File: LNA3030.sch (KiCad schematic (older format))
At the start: 25 parts, among them P1 SMA-KIT-1.5MF, U1 SWITCH, U2 SWITCH, U3 LNA, U4 SAW

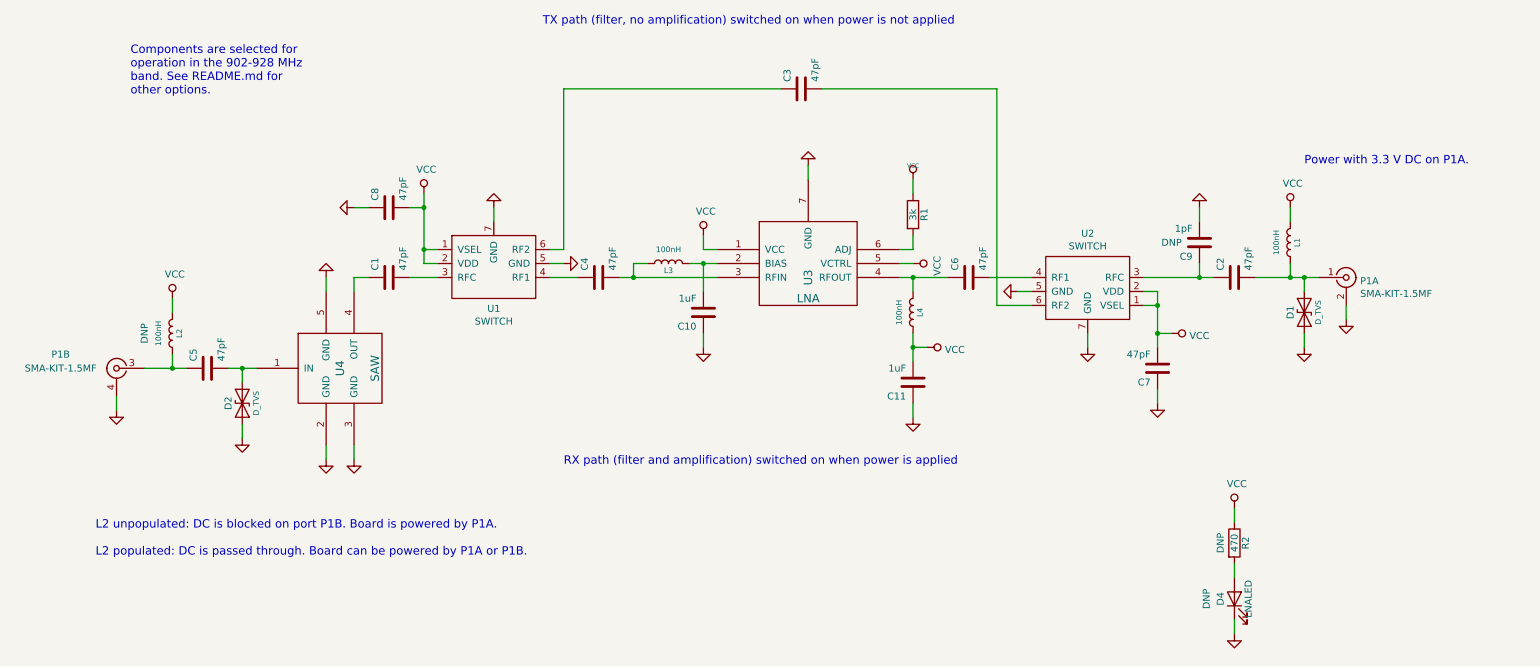
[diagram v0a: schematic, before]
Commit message: modify for DCC6C SAW filters
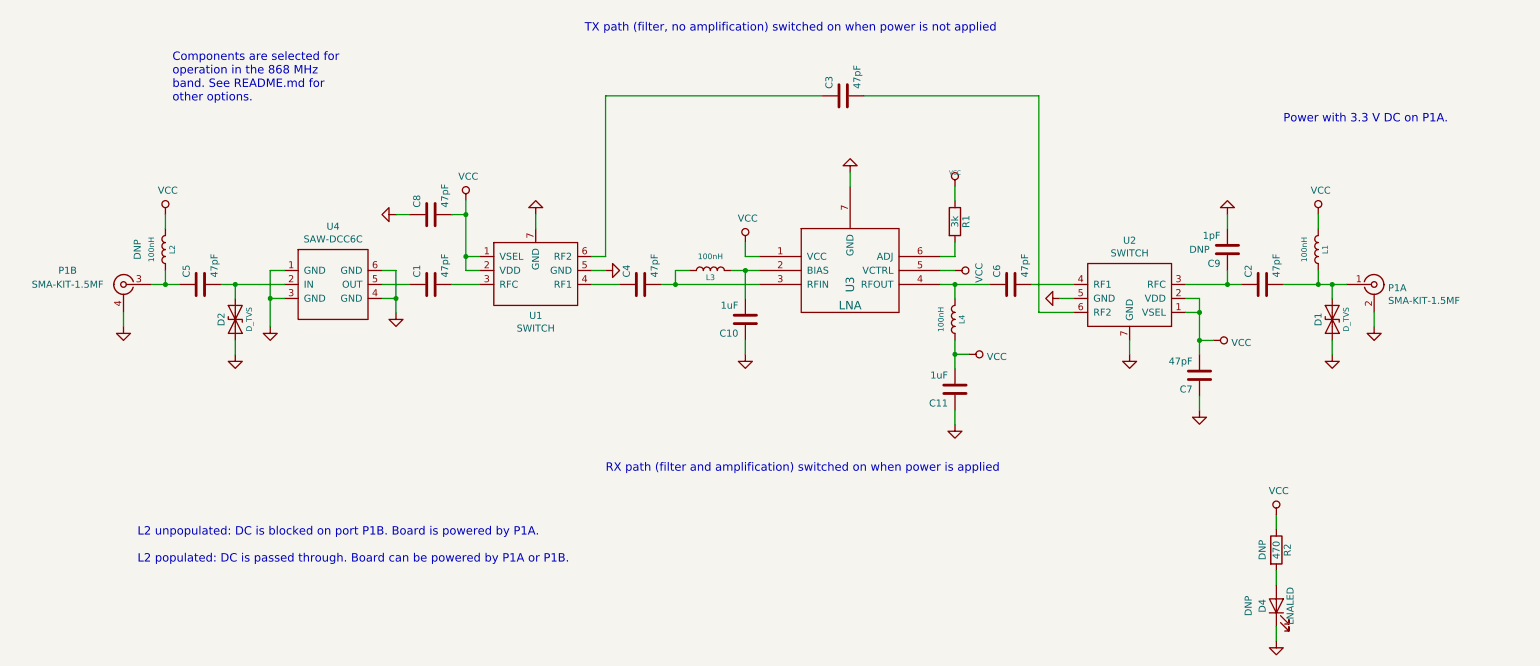
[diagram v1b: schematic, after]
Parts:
- removed U4: SAW, gsg-modules:F5Q, symbol gsg-symbols:FAR-F5QA
- added U4: SAW-DCC6C, LNA3030:DCC6C, symbol LNA3030:SAW-DCC6C
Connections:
- net GND: now also U4.1 (GND), U4.3 (GND), U4.4 (GND), U4.6 (GND)
- net at C5.2, D2.2 (A2): now also U4.2 (IN)
- net at C1.1: now also U4.5 (OUT)
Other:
- note added: "Components are selected for\noperation in the 868 MHz\nband. See README.md for\nother options."
- note removed: "Components are selected for\noperation in the 902-928 MHz\nband. See README.md for\nother options."
- moved on the sheet: C1, C10, C11, C2, C3, C4, C5, C6, C7, C8, C9, D1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

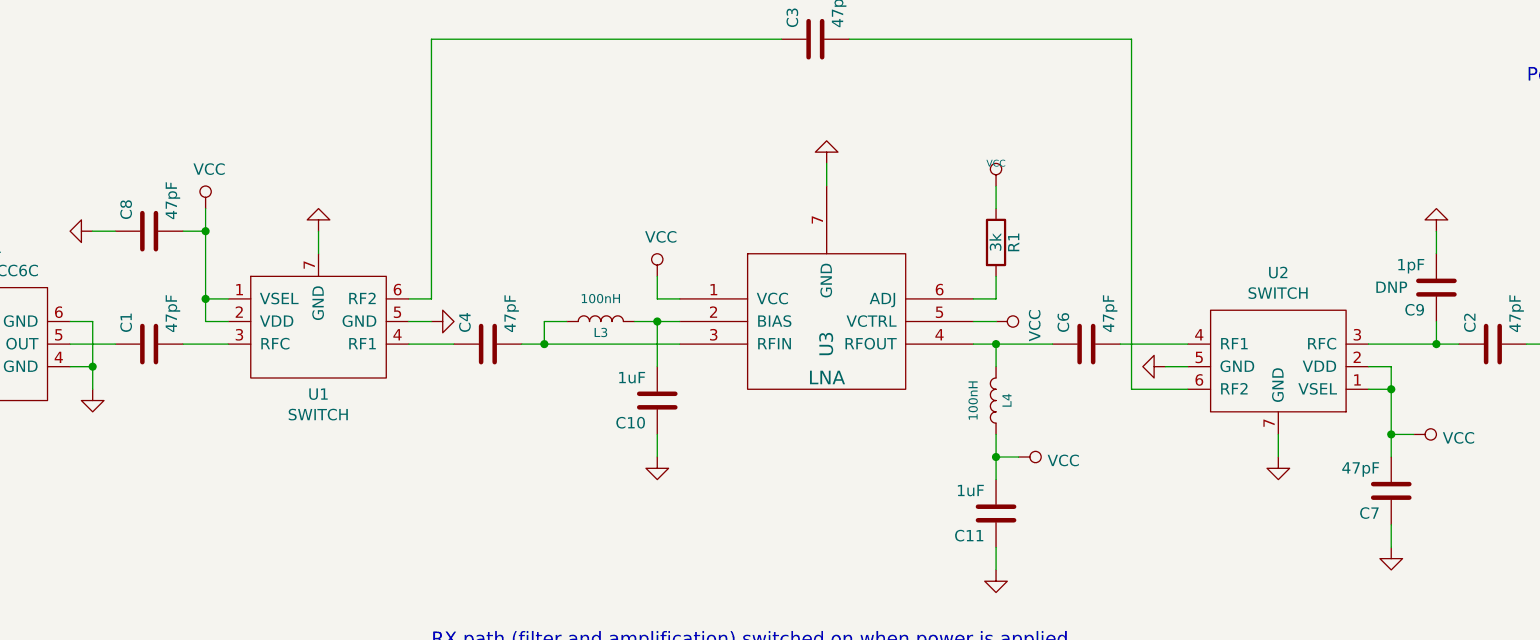
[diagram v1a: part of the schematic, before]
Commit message: correct C7 and C8 part selection
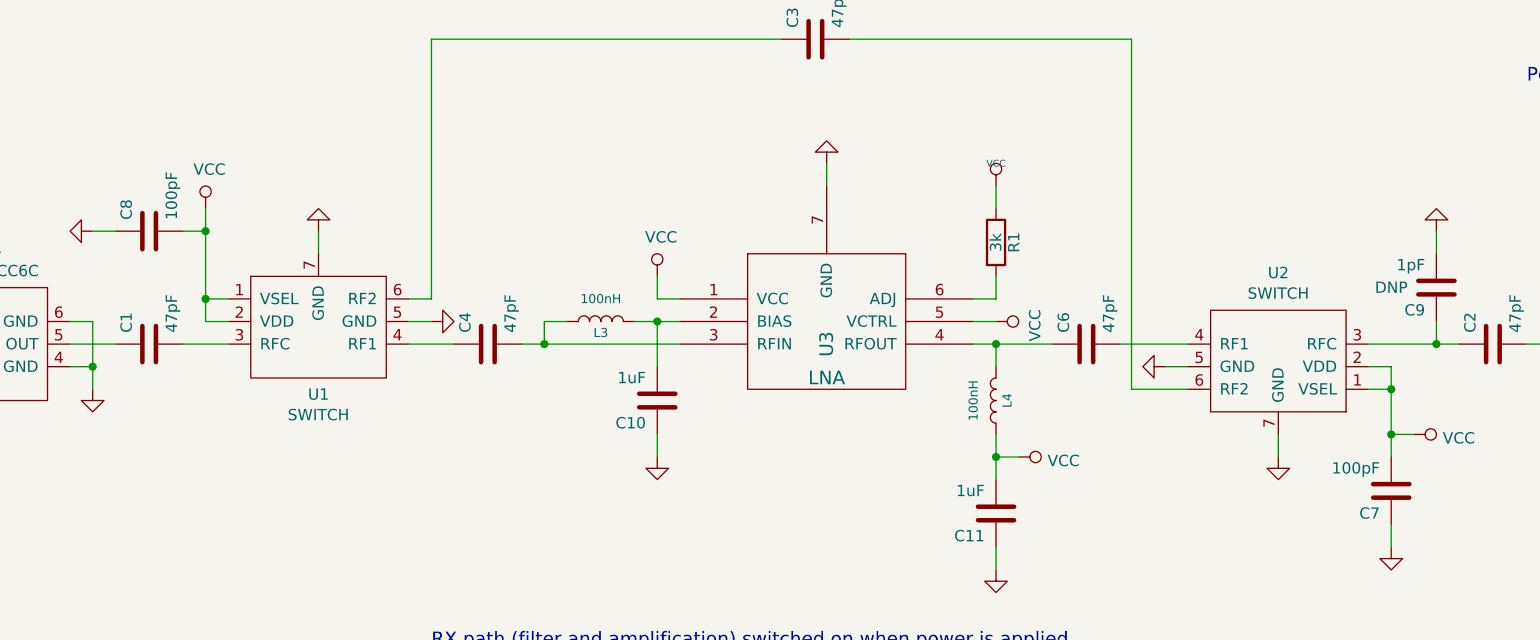
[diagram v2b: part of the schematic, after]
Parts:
- C7, C8: value 47pF -> 100pF; Description CAP CER 47PF 50V C0G/NP0 0402 -> CAP CER 100PF 50V 5% NP0 0402; Part Number GCM1555C1H470JA16D -> GCM1555C1H101JA16D
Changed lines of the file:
@@
 P 9050 3950
 F 0 "C7" H 9100 4050 50  0000 L CNN
-F 1 "47pF" H 9100 3850 50  0000 L CNN
+F 1 "100pF" H 9100 3850 50  0000 L CNN
 F 2 "gsg-modules:0402" H 9050 3950 50  0001 C CNN
 F 3 "" H 9050 3950 50  0001 C CNN
 F 4 "Murata" H 9050 3950 60  0001 C CNN "Manufacturer"
-F 5 "GCM1555C1H470JA16D" H 9050 3950 60  0001 C CNN "Part Number"
-F 6 "CAP CER 47PF 50V C0G/NP0 0402" H 9050 3950 60  0001 C CNN "Description"
+F 5 "GCM1555C1H101JA16D" H 9050 3950 60  0001 C CNN "Part Number"
+F 6 "CAP CER 100PF 50V 5% NP0 0402" H 9050 3950 60  0001 C CNN "Description"
 	1    9050 3950
 	-1   0    0    1
@@
 P 3550 2800
 F 0 "C8" H 3600 2900 50  0000 L CNN
-F 1 "47pF" H 3600 2700 50  0000 L CNN
+F 1 "100pF" H 3600 2700 50  0000 L CNN
 F 2 "gsg-modules:0402" H 3550 2800 50  0001 C CNN
 F 3 "" H 3550 2800 50  0001 C CNN
 F 4 "Murata" H 3550 2800 60  0001 C CNN "Manufacturer"
-F 5 "GCM1555C1H470JA16D" H 3550 2800 60  0001 C CNN "Part Number"
-F 6 "CAP CER 47PF 50V C0G/NP0 0402" H 3550 2800 60  0001 C CNN "Description"
+F 5 "GCM1555C1H101JA16D" H 3550 2800 60  0001 C CNN "Part Number"
+F 6 "CAP CER 100PF 50V 5% NP0 0402" H 3550 2800 60  0001 C CNN "Description"
 	1    3550 2800
 	0    -1   -1   0
